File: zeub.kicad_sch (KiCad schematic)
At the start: 18 parts, among them J1 debug-port, J2 OLED-128x64, Q1 AO3401A, Q2 AO3401A, Q3 AO3401A, Q4 AO3401A, SW1 SKRHA, SW2 RotaryEncoder_Switch, U5 holyiot-18010-no-underside, U6 MT25QL128ABA1ESE

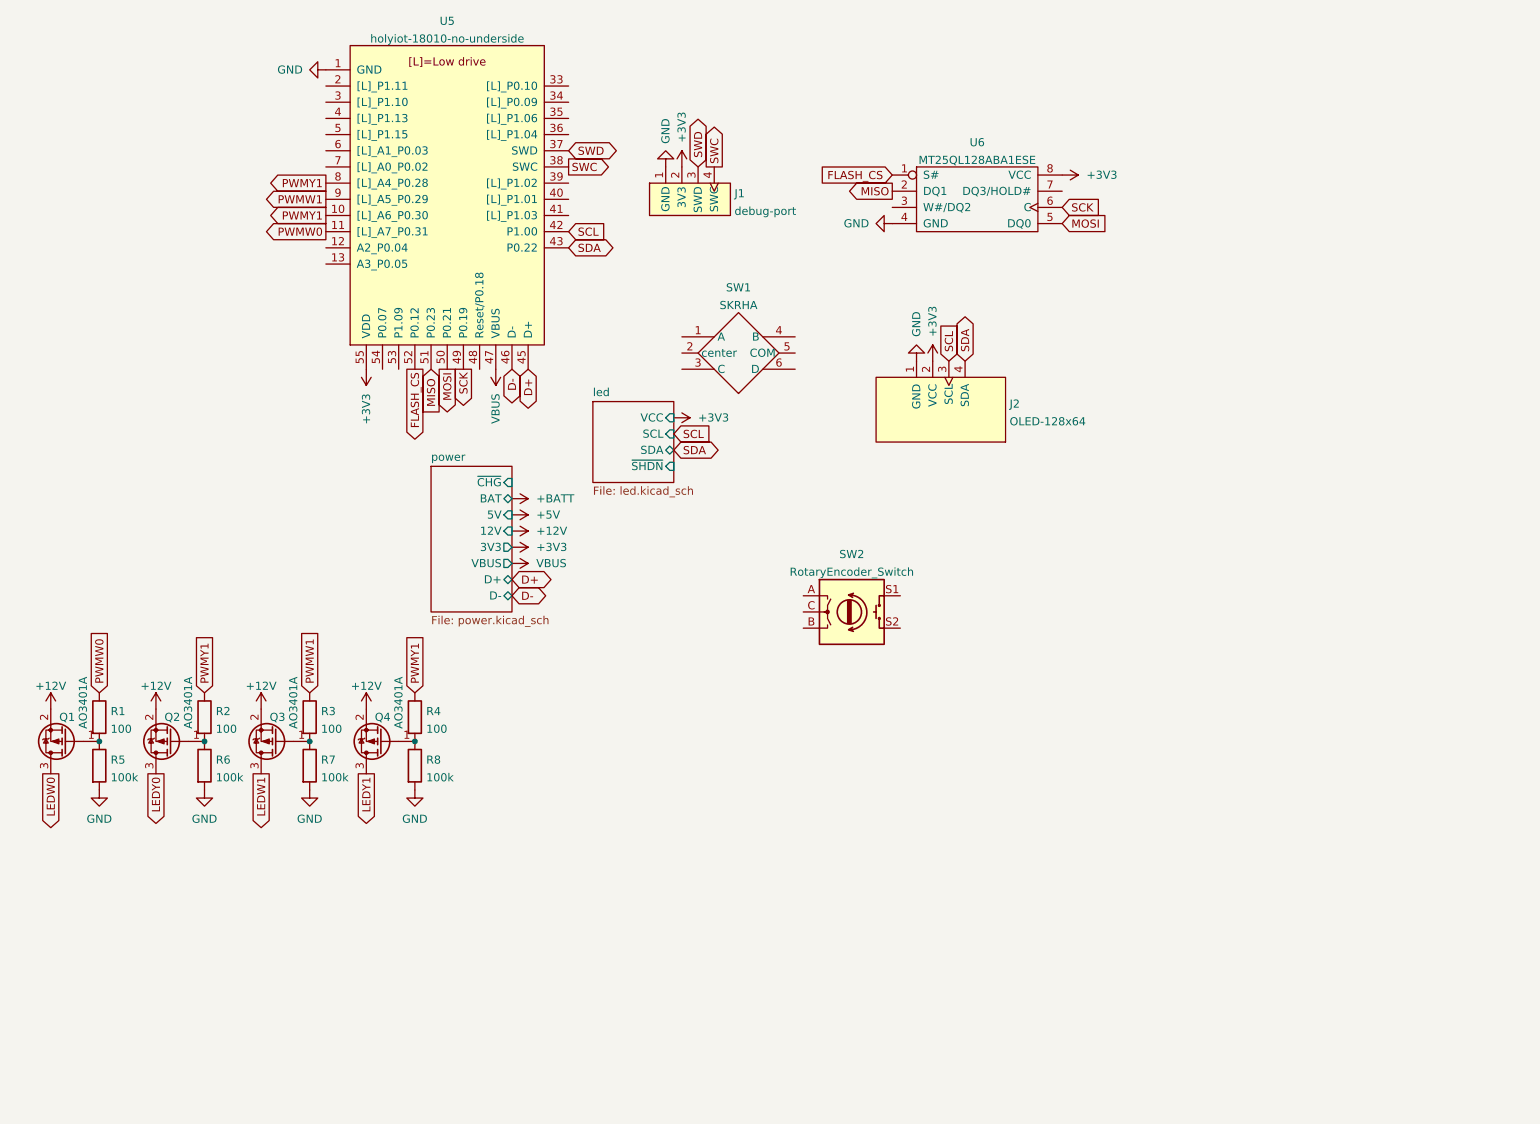
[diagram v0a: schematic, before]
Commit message: routed matrix + PWM driver
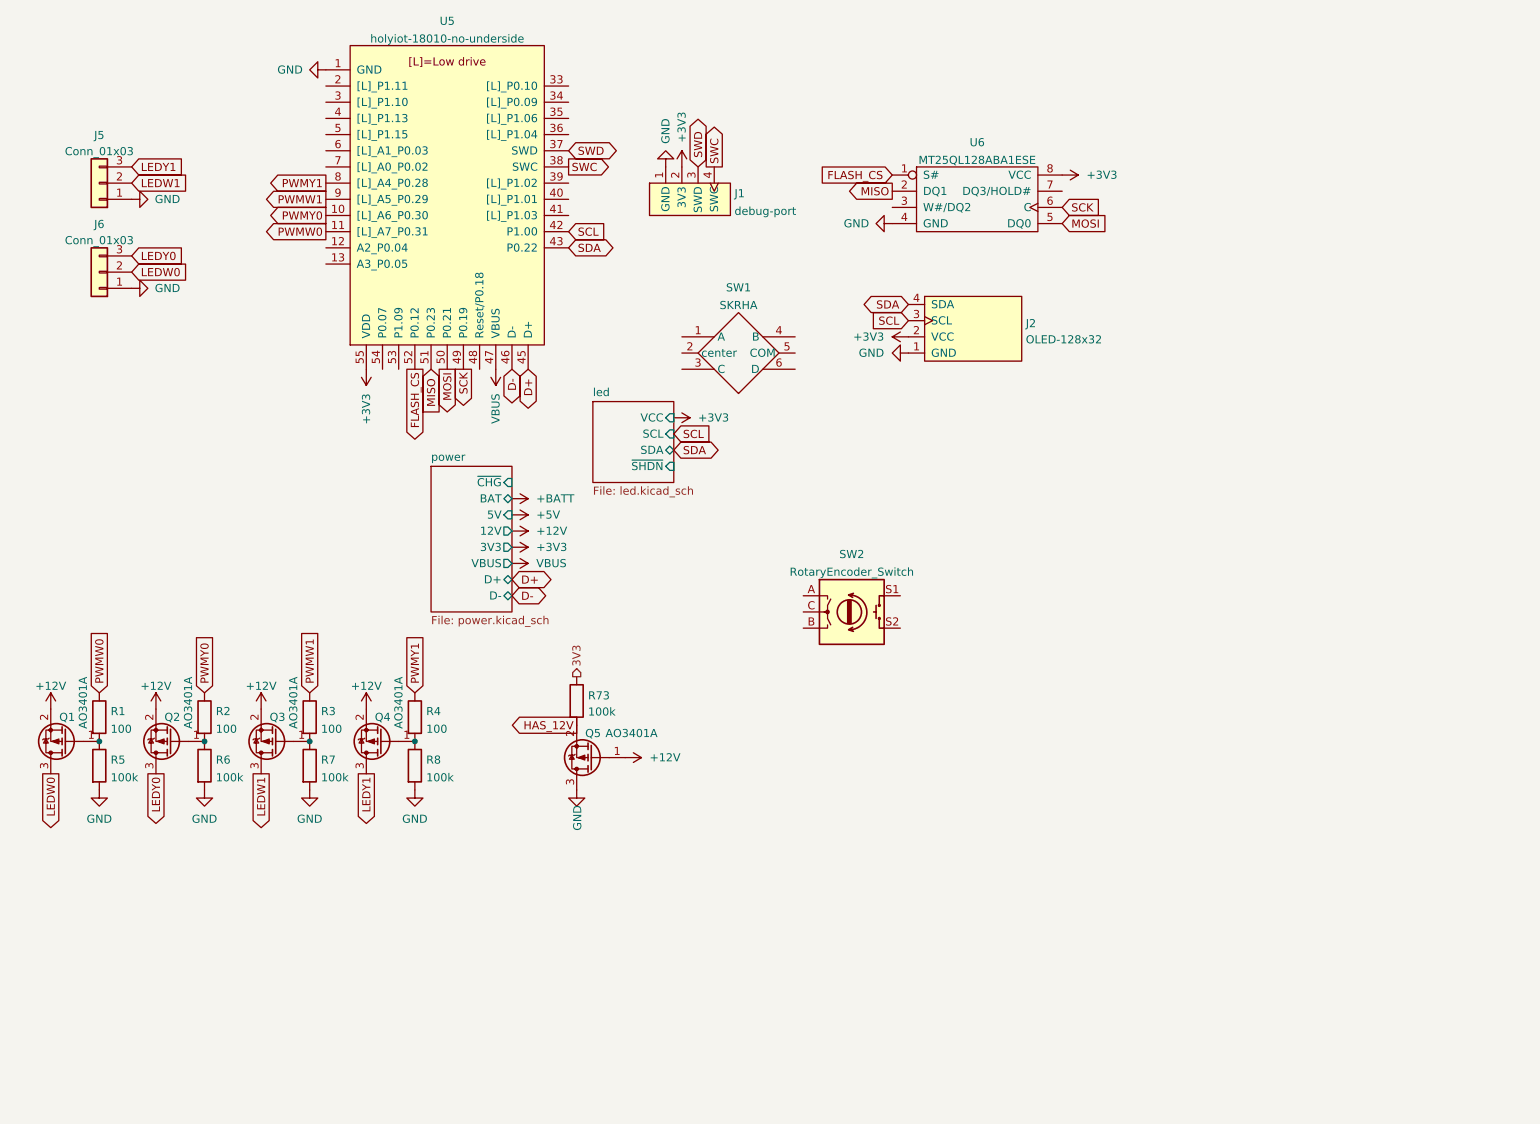
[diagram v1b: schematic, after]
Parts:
- removed J2: OLED-128x64, display:OLED-128x64, symbol display:OLED-128x64
- added J2: OLED-128x32, display:OLED-128x32-cutout, symbol display:OLED-128x32
- added J5, J6: Conn_01x03, Connector_PinHeader_2.54mm:PinHeader_1x03_P2.54mm_Vertical, symbol Connector_Generic:Conn_01x03
- added Q5: AO3401A, Package_TO_SOT_SMD:SOT-23, symbol Transistor_FET:AO3401A
- added R73: 100k, Resistor_SMD:R_0603_1608Metric, symbol Device:R
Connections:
- net +12V: now also Q5.1 (G)
- net +3V3: now also J2.2 (VCC)
- net GND: now also J2.1 (GND), J5.1 (Pin_1), J6.1 (Pin_1), Q5.3 (D)
- net LEDW0: now also J6.2 (Pin_2)
- net LEDW1: now also J5.2 (Pin_2)
- net LEDY0: now also J6.3 (Pin_3)
- net LEDY1: now also J5.3 (Pin_3)
- net PWMY1: no longer R2.1, U5.10 ([L]_A6_P0.30)
- net SCL: now also J2.3 (SCL)
- net SDA: now also J2.4 (SDA)
- new net 3V3: R73.1
- new net HAS_12V: Q5.2 (S), R73.2
- new net PWMY0: R2.1, U5.10 ([L]_A6_P0.30)

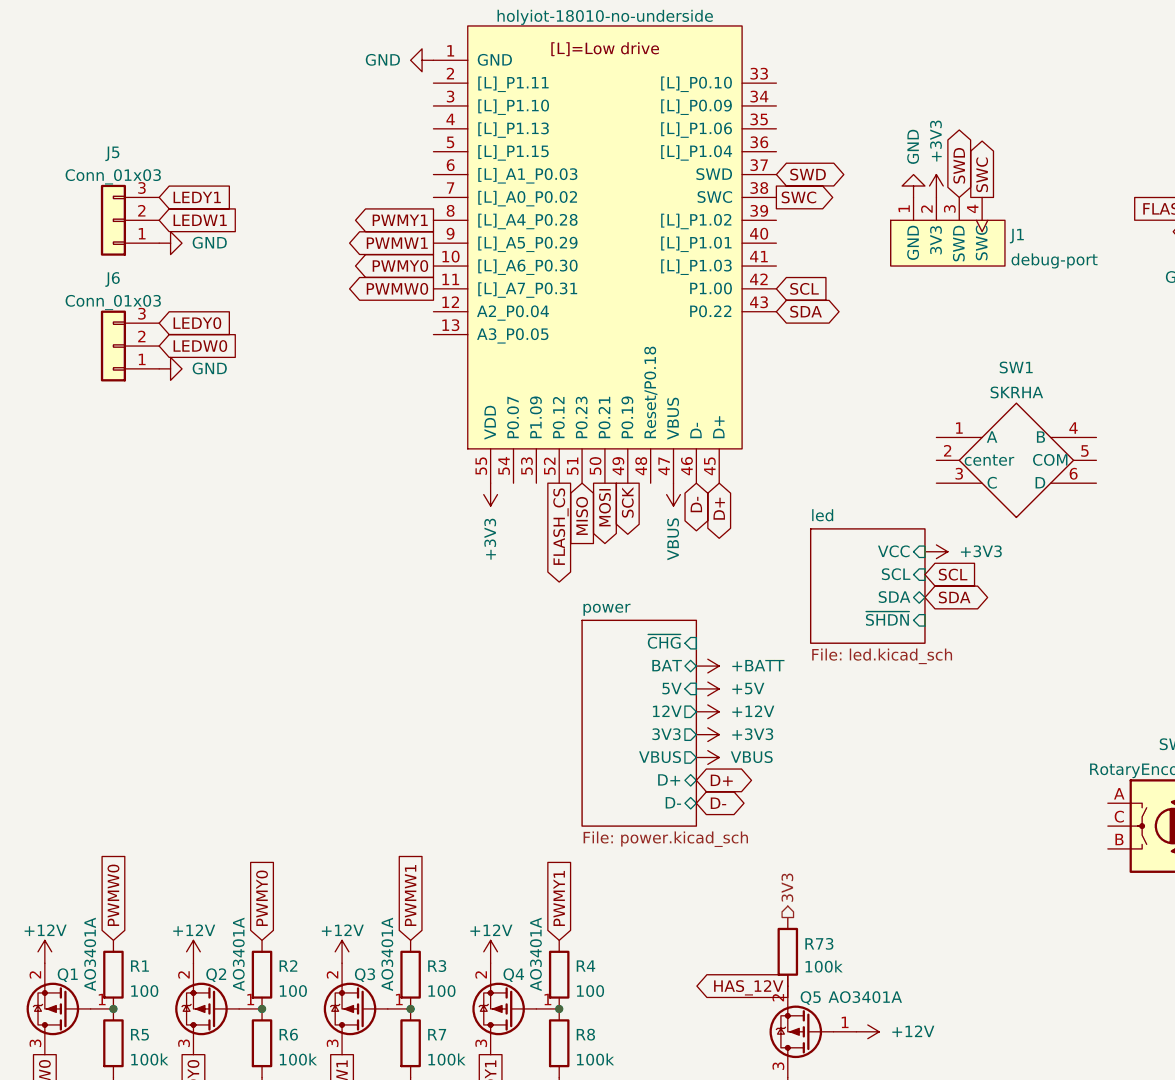
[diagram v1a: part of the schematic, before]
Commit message: routed PMU
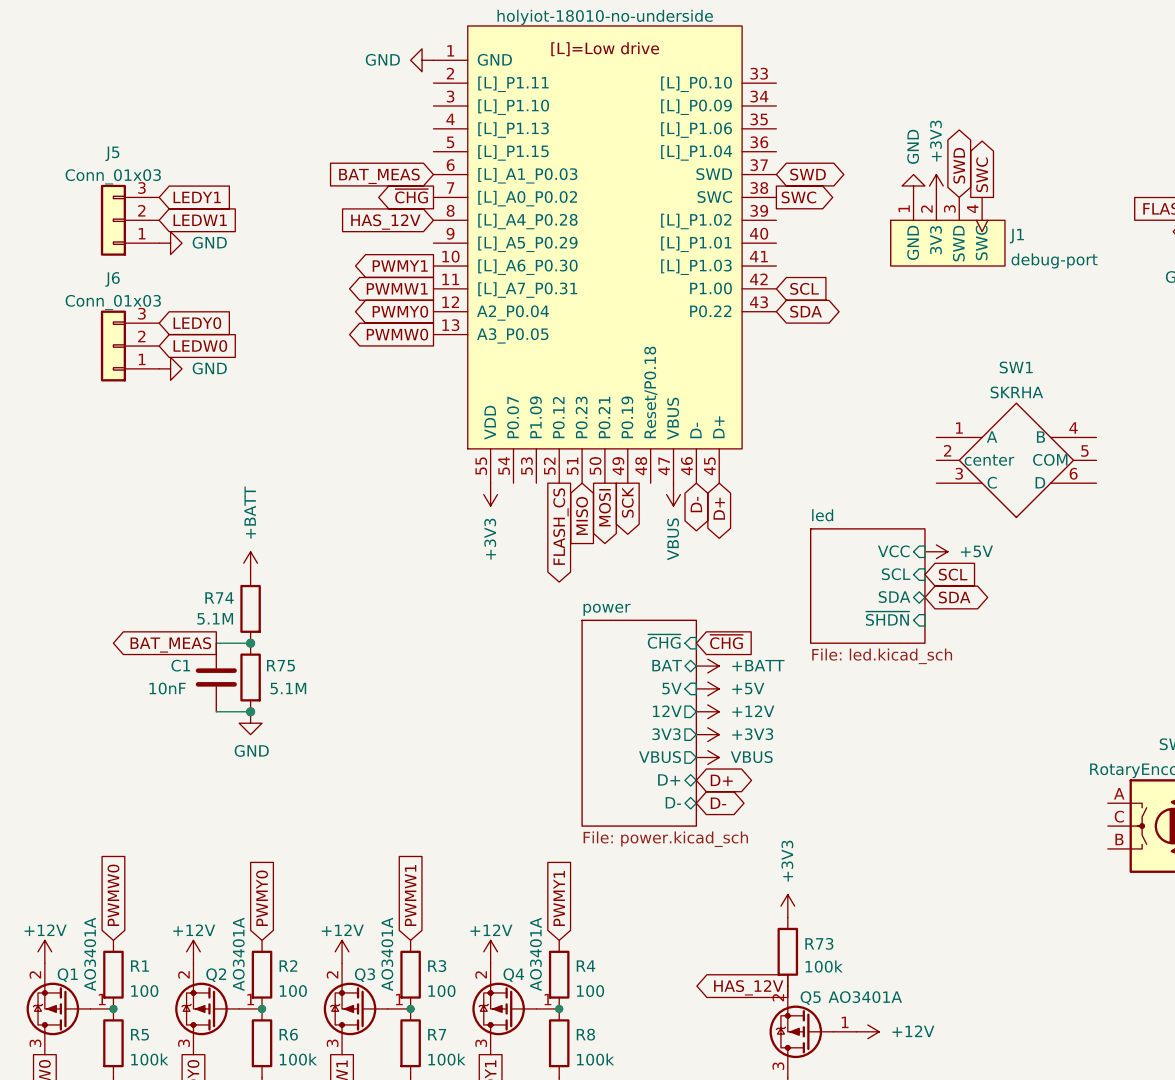
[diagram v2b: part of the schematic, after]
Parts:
- added C1: 10nF, Capacitor_SMD:C_0603_1608Metric, symbol Device:C
- added R74, R75: 5.1M, Resistor_SMD:R_0603_1608Metric, symbol Device:R
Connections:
- net 3V3 is gone; now on net +3V3: R73.1
- net +BATT: now also R74.1
- net GND: now also C1.2, R75.2
- net HAS_12V: now also U5.8 ([L]_A4_P0.28)
- net PWMW0: now also U5.13 (A3_P0.05); no longer U5.11 ([L]_A7_P0.31)
- net PWMW1: now also U5.11 ([L]_A7_P0.31); no longer U5.9 ([L]_A5_P0.29)
- net PWMY0: now also U5.12 (A2_P0.04); no longer U5.10 ([L]_A6_P0.30)
- net PWMY1: now also U5.10 ([L]_A6_P0.30); no longer U5.8 ([L]_A4_P0.28)
- net BAT_MEAS: now reaches U5.6 ([L]_A1_P0.03)
- net BAT_MEAS: now also C1.1, R74.2, R75.1
- net ~{CHG}: now reaches U5.7 ([L]_A0_P0.02)
